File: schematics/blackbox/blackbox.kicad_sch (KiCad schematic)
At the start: 31 parts, among them J1 Micro_SD_Card, J104 SWD, J105 F_COMPUTER, J2 Micro_SD_Card, U101 MAX14787E, U102 STM32F405RGT6, Y101 26M

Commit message: Add power LED and test points
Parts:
- added D101: RED, Strix:LED_0402, symbol Strix:LED
- added R101: 50, Strix:R_0402, symbol Strix:R
- added TP101, TP102, TP103, TP104, TP105, TP106, TP107, TP108, TP109, TP110, TP111, TP112, TP113, TP114, TP115: TestPoint, Strix:TestPoint, symbol Strix:TestPoint
- renumbered C105 to C102, C107 to C103, C112 to C104, C102 to C105, C108 to C107, C109 to C108, C110 to C109, C111 to C110, C103 to C111, C104 to C112, D104 to D102, D105 to D103, D106 to D104, D107 to D105, D108 to D106, D109 to D107, J1 to J101, J2 to J102, J104 to J103, J105 to J104, R101 to R103, U102 to U101, U101 to U102
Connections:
- net 3v3: now also R101.2, TP109.1
- net GND: now also D101.1, TP112.1, TP113.1, TP114.1, TP115.1
- net SD1_~{CS}: now also TP101.1
- net SD2_~{CS}: now also TP102.1
- net SPI2_MISO: now also TP110.1
- net SPI2_MOSI: now also TP107.1
- net SPI2_SCLK: now also TP104.1
- net SPI3_MISO: now also TP111.1
- net SPI3_MOSI: now also TP108.1
- net SPI3_SCLK: now also TP105.1
- net USART3_RX: now also TP103.1
- net USART3_TX: now also TP106.1
- new net: D101.2, R101.1
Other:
- note added: "Power LED"
- note added: "Test Points"

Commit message: Final changes for manufacture (and silkscreen meme)
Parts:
- C101: Farnell 2496814 -> 1759436
- C104: Farnell 2426952 -> 2211173
- C111, C112: Farnell (none) -> 2494183
- J101, J102: Farnell (none) -> 1344008
- J103: Farnell (none) -> 2856426
- R101: Farnell (none) -> 3544456
- R102: Farnell (none) -> 2447095
- R103: Farnell (none) -> 2447103
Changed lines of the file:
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@@
       (effects (font (size 1.27 1.27)) hide)
     )
-    (property "Farnell" "2496814" (id 4) (at 76.2 66.04 0)
+    (property "Farnell" "1759436" (id 4) (at 76.2 66.04 0)
       (effects (font (size 1.27 1.27)) hide)
     )
@@
       (effects (font (size 1.27 1.27)) hide)
     )
-    (property "Farnell" "2426952" (id 4) (at 119.38 72.39 0)
+    (property "Farnell" "2211173" (id 4) (at 119.38 72.39 0)
       (effects (font (size 1.27 1.27)) hide)
     )
@@
     )
     (property "Datasheet" "~" (id 3) (at 146.05 179.07 0)
+      (effects (font (size 1.27 1.27)) hide)
+    )
+    (property "Farnell" "~" (id 4) (at 146.05 179.07 0)
       (effects (font (size 1.27 1.27)) hide)
     )
@@
       (effects (font (size 1.27 1.27)) hide)
     )
+    (property "Farnell" "~" (id 4) (at 153.67 179.07 0)
+      (effects (font (size 1.27 1.27)) hide)
+    )
     (pin "1")
   )
@@
       (effects (font (size 1.27 1.27)) hide)
     )
+    (property "Farnell" "~" (id 4) (at 161.29 179.07 0)
+      (effects (font (size 1.27 1.27)) hide)
+    )
     (pin "1")
   )
@@
     )
     (property "Datasheet" "~" (id 3) (at 168.91 179.07 0)
+      (effects (font (size 1.27 1.27)) hide)
+    )
+    (property "Farnell" "~" (id 4) (at 168.91 179.07 0)
       (effects (font (size 1.27 1.27)) hide)
     )
@@
       (effects (font (size 1.27 1.27)) hide)
     )
+    (property "Farnell" "2447103" (id 4) (at 53.34 177.8 0)
+      (effects (font (size 1.27 1.27)) hide)
+    )
     (pin "1")
     (pin "2")
@@
       (effects (font (size 1.27 1.27)) hide)
     )
+    (property "Farnell" "~" (id 4) (at 153.67 35.56 0)
+      (effects (font (size 1.27 1.27)) hide)
+    )
     (pin "1")
   )
@@
     )
     (property "Datasheet" "~" (id 3) (at 153.67 50.8 0)
+      (effects (font (size 1.27 1.27)) hide)
+    )
+    (property "Farnell" "~" (id 4) (at 153.67 45.72 0)
       (effects (font (size 1.27 1.27)) hide)
     )
@@
       (effects (font (size 1.27 1.27)) hide)
     )
+    (property "Farnell" "3544456" (id 4) (at 59.69 68.58 0)
+      (effects (font (size 1.27 1.27)) hide)
+    )
     (pin "1")
     (pin "2")
@@
     )
     (property "Datasheet" "~" (id 3) (at 153.67 48.26 0)
+      (effects (font (size 1.27 1.27)) hide)
+    )
+    (property "Farnell" "~" (id 4) (at 153.67 43.18 0)
       (effects (font (size 1.27 1.27)) hide)
     )
@@
     )
     (property "Datasheet" "http://katalog.we-online.de/em/datasheet/693072010801.pdf" (id 3) (at 224.79 123.19 0)
+      (effects (font (size 1.27 1.27)) hide)
+    )
+    (property "Farnell" "1344008" (id 4) (at 224.79 123.19 0)
       (effects (font (size 1.27 1.27)) hide)
     )
@@
       (effects (font (size 1.27 1.27)) hide)
     )
+    (property "Farnell" "2494183" (id 4) (at 81.28 113.03 0)
+      (effects (font (size 1.27 1.27)) hide)
+    )
     (pin "1")
     (pin "2")
@@
       (effects (font (size 1.27 1.27)) hide)
     )
+    (property "Farnell" "2447095" (id 4) (at 88.9 110.49 0)
+      (effects (font (size 1.27 1.27)) hide)
+    )
     (pin "1")
     (pin "2")
@@
       (effects (font (size 1.27 1.27)) hide)
     )
+    (property "Farnell" "~" (id 4) (at 92.71 40.64 0)
+      (effects (font (size 1.27 1.27)) hide)
+    )
     (pin "1")
   )
@@
       (effects (font (size 1.27 1.27)) hide)
     )
+    (property "Farnell" "~" (id 4) (at 153.67 40.64 0)
+      (effects (font (size 1.27 1.27)) hide)
+    )
     (pin "1")
   )
@@
     )
     (property "Datasheet" "~" (id 3) (at 92.71 50.8 0)
+      (effects (font (size 1.27 1.27)) hide)
+    )
+    (property "Farnell" "~" (id 4) (at 92.71 45.72 0)
       (effects (font (size 1.27 1.27)) hide)
     )
@@
       (effects (font (size 1.27 1.27)) hide)
     )
+    (property "Farnell" "~" (id 4) (at 123.19 45.72 0)
+      (effects (font (size 1.27 1.27)) hide)
+    )
     (pin "1")
   )
@@
     )
     (property "Datasheet" "~" (id 3) (at 92.71 43.18 0)
+      (effects (font (size 1.27 1.27)) hide)
+    )
+    (property "Farnell" "~" (id 4) (at 92.71 38.1 0)
       (effects (font (size 1.27 1.27)) hide)
     )
@@
     )
     (property "Datasheet" "http://katalog.we-online.de/em/datasheet/693072010801.pdf" (id 3) (at 224.79 83.82 0)
+      (effects (font (size 1.27 1.27)) hide)
+    )
+    (property "Farnell" "1344008" (id 4) (at 224.79 83.82 0)
       (effects (font (size 1.27 1.27)) hide)
     )
@@
       (effects (font (size 1.27 1.27)) hide)
     )
+    (property "Farnell" "~" (id 4) (at 123.19 40.64 0)
+      (effects (font (size 1.27 1.27)) hide)
+    )
     (pin "1")
   )
@@
       (effects (font (size 1.27 1.27)) hide)
     )
+    (property "Farnell" "~" (id 4) (at 123.19 35.56 0)
+      (effects (font (size 1.27 1.27)) hide)
+    )
     (pin "1")
   )
@@
     )
     (property "Datasheet" "~" (id 3) (at 123.19 43.18 0)
+      (effects (font (size 1.27 1.27)) hide)
+    )
+    (property "Farnell" "~" (id 4) (at 123.19 38.1 0)
       (effects (font (size 1.27 1.27)) hide)
     )
@@
       (effects (font (size 1.27 1.27)) hide)
     )
+    (property "Farnell" "2494183" (id 4) (at 81.28 102.87 0)
+      (effects (font (size 1.27 1.27)) hide)
+    )
     (pin "1")
     (pin "2")
@@
     )
     (property "Datasheet" "~" (id 3) (at 92.71 40.64 0)
+      (effects (font (size 1.27 1.27)) hide)
+    )
+    (property "Farnell" "~" (id 4) (at 92.71 35.56 0)
       (effects (font (size 1.27 1.27)) hide)
     )
@@
       (effects (font (size 1.27 1.27)) hide)
     )
+    (property "Farnell" "~" (id 4) (at 153.67 38.1 0)
+      (effects (font (size 1.27 1.27)) hide)
+    )
     (pin "1")
   )
@@
     )
     (property "Datasheet" "~" (id 3) (at 123.19 48.26 0)
+      (effects (font (size 1.27 1.27)) hide)
+    )
+    (property "Farnell" "~" (id 4) (at 123.19 43.18 0)
       (effects (font (size 1.27 1.27)) hide)
     )
@@
     )
     (property "Datasheet" "~" (id 3) (at 102.87 177.8 0)
+      (effects (font (size 1.27 1.27)) hide)
+    )
+    (property "Farnell" "~" (id 4) (at 102.87 177.8 0)
       (effects (font (size 1.27 1.27)) hide)
     )
@@
     )
     (property "Datasheet" "~" (id 3) (at 78.74 142.24 0)
+      (effects (font (size 1.27 1.27)) hide)
+    )
+    (property "Farnell" "2856426" (id 4) (at 78.74 142.24 0)
       (effects (font (size 1.27 1.27)) hide)
     )
@@
       (effects (font (size 1.27 1.27)) hide)
     )
+    (property "Farnell" "~" (id 4) (at 92.71 43.18 0)
+      (effects (font (size 1.27 1.27)) hide)
+    )

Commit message: Fix library references
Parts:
- J101, J102: footprint Connector_Card:microSD_HC_Wuerth_693072010801 -> Strix:microSD_HC_Wuerth_693072010801; symbol Connector:Micro_SD_Card -> Strix:Micro_SD_Card
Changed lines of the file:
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@@
     (pin "1")
   )
-  (symbol (lib_id "Connector:Micro_SD_Card") (at 224.79 123.19 0) (unit 1)
+  (symbol (lib_id "Strix:Micro_SD_Card") (at 224.79 123.19 0) (unit 1)
     (in_bom yes) (on_board yes) (fields_autoplaced)
     (property "Reference" "J102" (id 0) (at 225.425 104.14 0))
     (property "Value" "Micro_SD_Card" (id 1) (at 225.425 106.68 0))
-    (property "Footprint" "Connector_Card:microSD_HC_Wuerth_693072010801" (id 2) (at 254 115.57 0)
+    (property "Footprint" "Strix:microSD_HC_Wuerth_693072010801" (id 2) (at 254 115.57 0)
       (effects (font (size 1.27 1.27)) hide)
     )
@@
     (pin "1")
   )
-  (symbol (lib_id "Connector:Micro_SD_Card") (at 224.79 83.82 0) (unit 1)
+  (symbol (lib_id "Strix:Micro_SD_Card") (at 224.79 83.82 0) (unit 1)
     (in_bom yes) (on_board yes) (fields_autoplaced)
     (property "Reference" "J101" (id 0) (at 225.425 64.77 0))
     (property "Value" "Micro_SD_Card" (id 1) (at 225.425 67.31 0))
-    (property "Footprint" "Connector_Card:microSD_HC_Wuerth_693072010801" (id 2) (at 254 76.2 0)
+    (property "Footprint" "Strix:microSD_HC_Wuerth_693072010801" (id 2) (at 254 76.2 0)
       (effects (font (size 1.27 1.27)) hide)
     )
@@
     )
     (path "/b9cca626-7245-4480-a9b4-98fe421cf0c1"
-      (reference "J101") (unit 1) (value "Micro_SD_Card") (footprint "Connector_Card:microSD_HC_Wuerth_693072010801")
+      (reference "J101") (unit 1) (value "Micro_SD_Card") (footprint "Strix:microSD_HC_Wuerth_693072010801")
     )
     (path "/44234758-a0aa-4225-a0d7-15a67df397a1"
-      (reference "J102") (unit 1) (value "Micro_SD_Card") (footprint "Connector_Card:microSD_HC_Wuerth_693072010801")
+      (reference "J102") (unit 1) (value "Micro_SD_Card") (footprint "Strix:microSD_HC_Wuerth_693072010801")
     )
     (path "/e584c80e-3de9-4f7a-9e9d-844bd2086241"

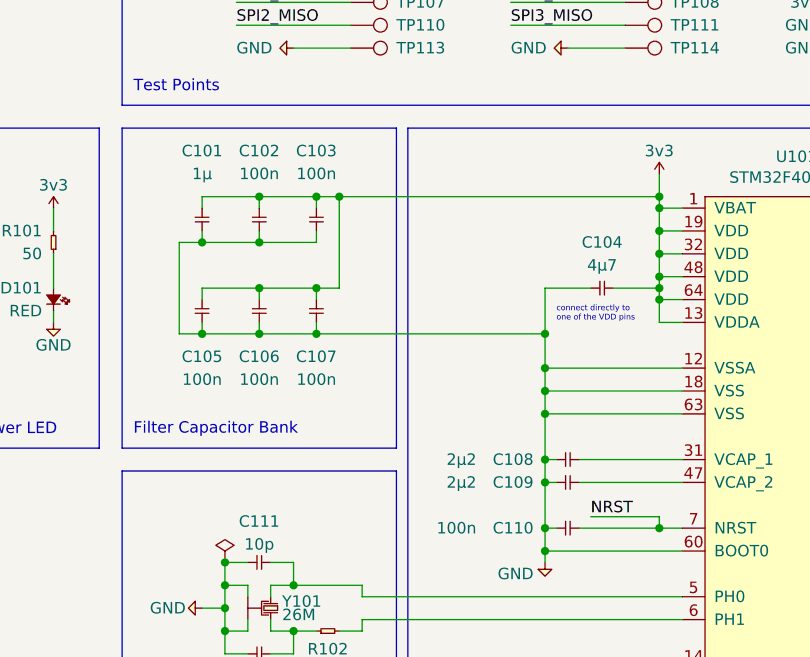
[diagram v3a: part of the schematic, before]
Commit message: Update passive order codes to 0402
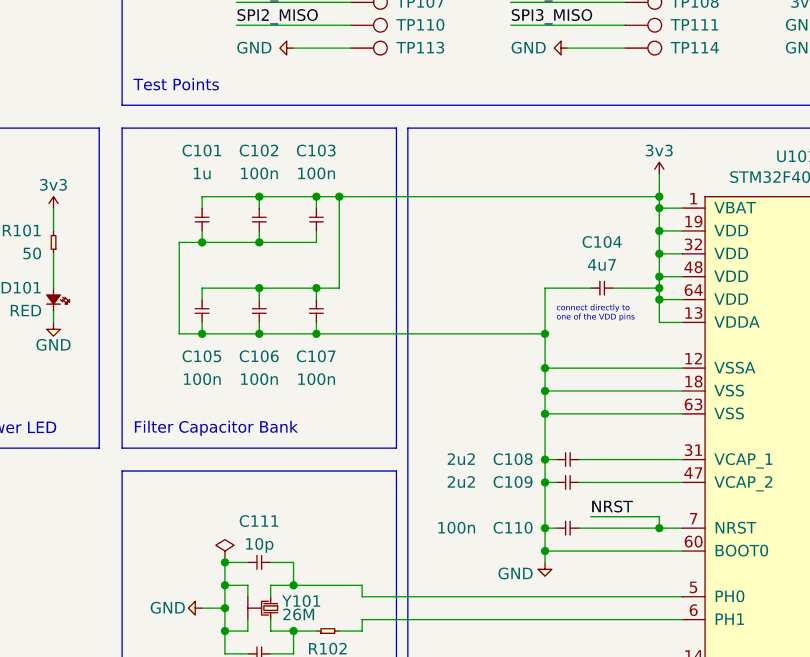
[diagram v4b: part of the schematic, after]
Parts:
- C101: value 1µ -> 1u; Farnell 1759436 -> 2218855
- C104: value 4µ7 -> 4u7; Farnell 2211173 -> 2346876
- C108, C109: value 2µ2 -> 2u2
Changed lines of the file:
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@@
       (effects (font (size 1.27 1.27)) (justify right))
     )
-    (property "Value" "2µ2" (id 1) (at 106.68 91.44 0)
+    (property "Value" "2u2" (id 1) (at 106.68 91.44 0)
       (effects (font (size 1.27 1.27)) (justify right))
     )
@@
       (effects (font (size 1.27 1.27)) (justify right))
     )
-    (property "Value" "2µ2" (id 1) (at 106.68 93.98 0)
+    (property "Value" "2u2" (id 1) (at 106.68 93.98 0)
       (effects (font (size 1.27 1.27)) (justify right))
     )
@@
     (in_bom yes) (on_board yes)
     (property "Reference" "C101" (id 0) (at 76.2 57.15 90))
-    (property "Value" "1µ" (id 1) (at 76.2 59.69 90))
+    (property "Value" "1u" (id 1) (at 76.2 59.69 90))
     (property "Footprint" "Strix:C_0402" (id 2) (at 76.2 66.04 0)
       (effects (font (size 1.27 1.27)) hide)
@@
       (effects (font (size 1.27 1.27)) hide)
     )
-    (property "Farnell" "1759436" (id 4) (at 76.2 66.04 0)
+    (property "Farnell" "2218855" (id 4) (at 76.2 66.04 0)
       (effects (font (size 1.27 1.27)) hide)
     )
@@
     (in_bom yes) (on_board yes)
     (property "Reference" "C104" (id 0) (at 120.65 67.31 0))
-    (property "Value" "4µ7" (id 1) (at 120.65 69.85 0))
+    (property "Value" "4u7" (id 1) (at 120.65 69.85 0))
     (property "Footprint" "Strix:C_0402" (id 2) (at 119.38 72.39 0)
       (effects (font (size 1.27 1.27)) hide)
@@
       (effects (font (size 1.27 1.27)) hide)
     )
-    (property "Farnell" "2211173" (id 4) (at 119.38 72.39 0)
+    (property "Farnell" "2346876" (id 4) (at 119.38 72.39 0)
       (effects (font (size 1.27 1.27)) hide)
     )
@@
     )
     (path "/00000000-0000-0000-0000-000060e7c4a9"
-      (reference "C101") (unit 1) (value "1µ") (footprint "Strix:C_0402")
+      (reference "C101") (unit 1) (value "1u") (footprint "Strix:C_0402")
     )
     (path "/00000000-0000-0000-0000-000060e7c4a2"
@@
     )
     (path "/00000000-0000-0000-0000-000060e7c4b0"
-      (reference "C104") (unit 1) (value "4µ7") (footprint "Strix:C_0402")
+      (reference "C104") (unit 1) (value "4u7") (footprint "Strix:C_0402")
     )
     (path "/00000000-0000-0000-0000-000060e7c494"
@@
     )
     (path "/00000000-0000-0000-0000-000060e7c46a"
-      (reference "C108") (unit 1) (value "2µ2") (footprint "Strix:C_0402")
+      (reference "C108") (unit 1) (value "2u2") (footprint "Strix:C_0402")
     )
     (path "/00000000-0000-0000-0000-000060e7c471"
-      (reference "C109") (unit 1) (value "2µ2") (footprint "Strix:C_0402")
+      (reference "C109") (unit 1) (value "2u2") (footprint "Strix:C_0402")
     )
     (path "/00000000-0000-0000-0000-0000613d0152"

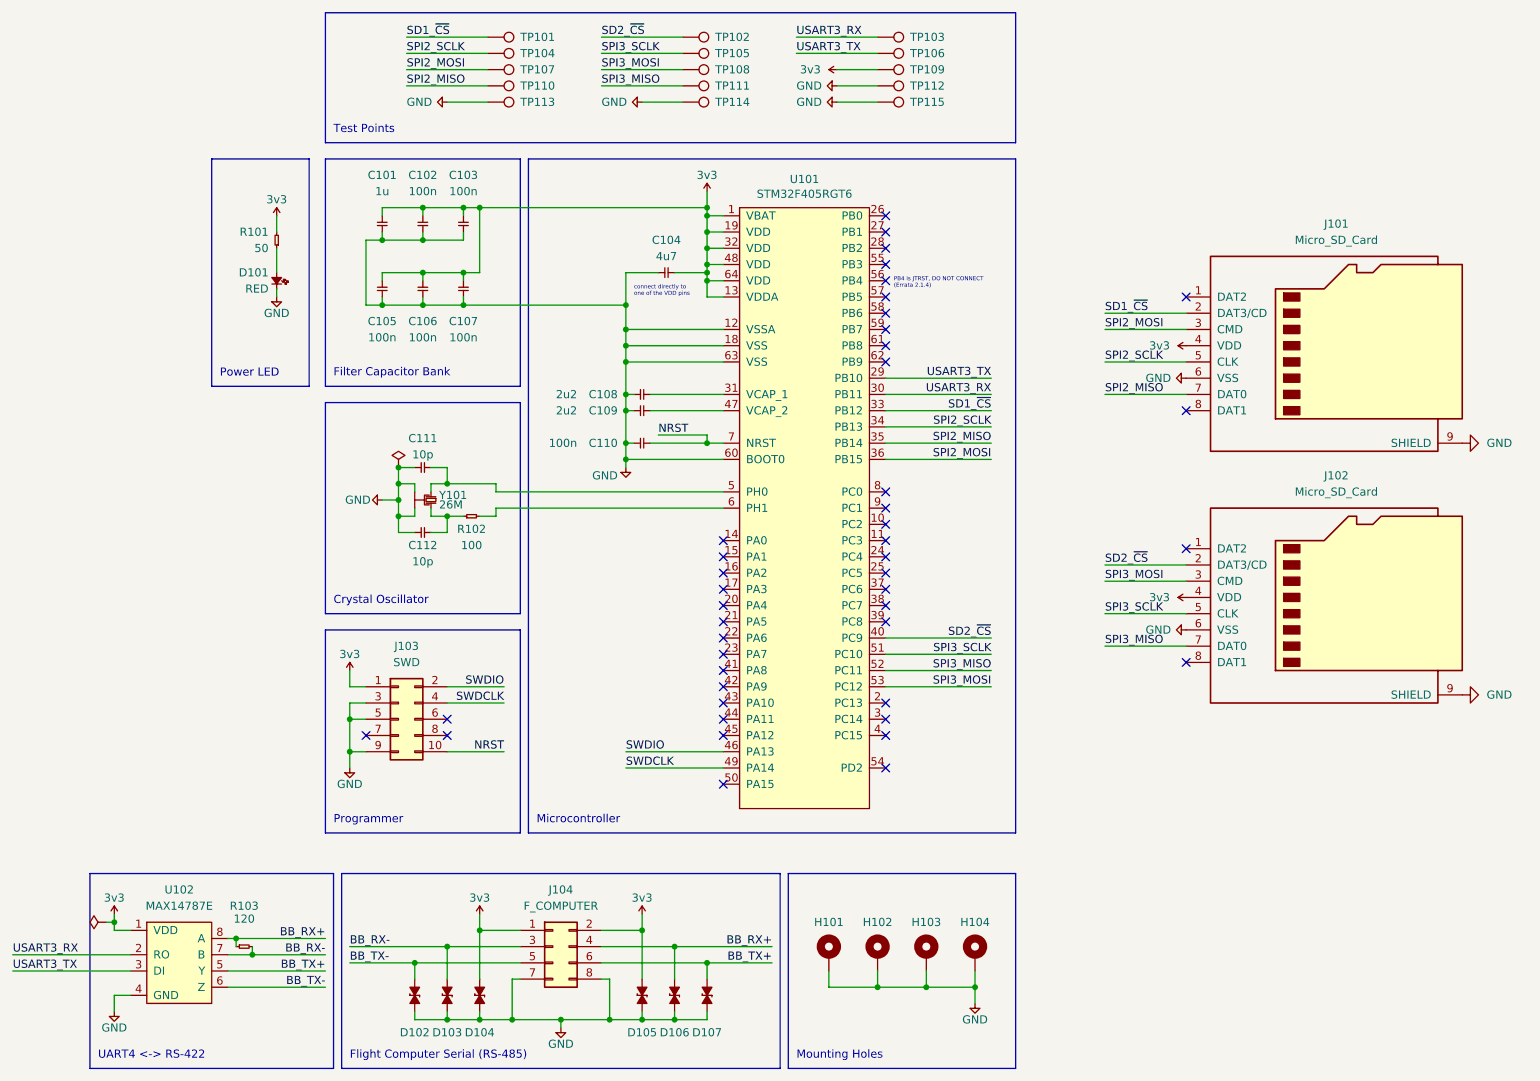
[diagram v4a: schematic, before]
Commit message: Minor changes to pass ERC
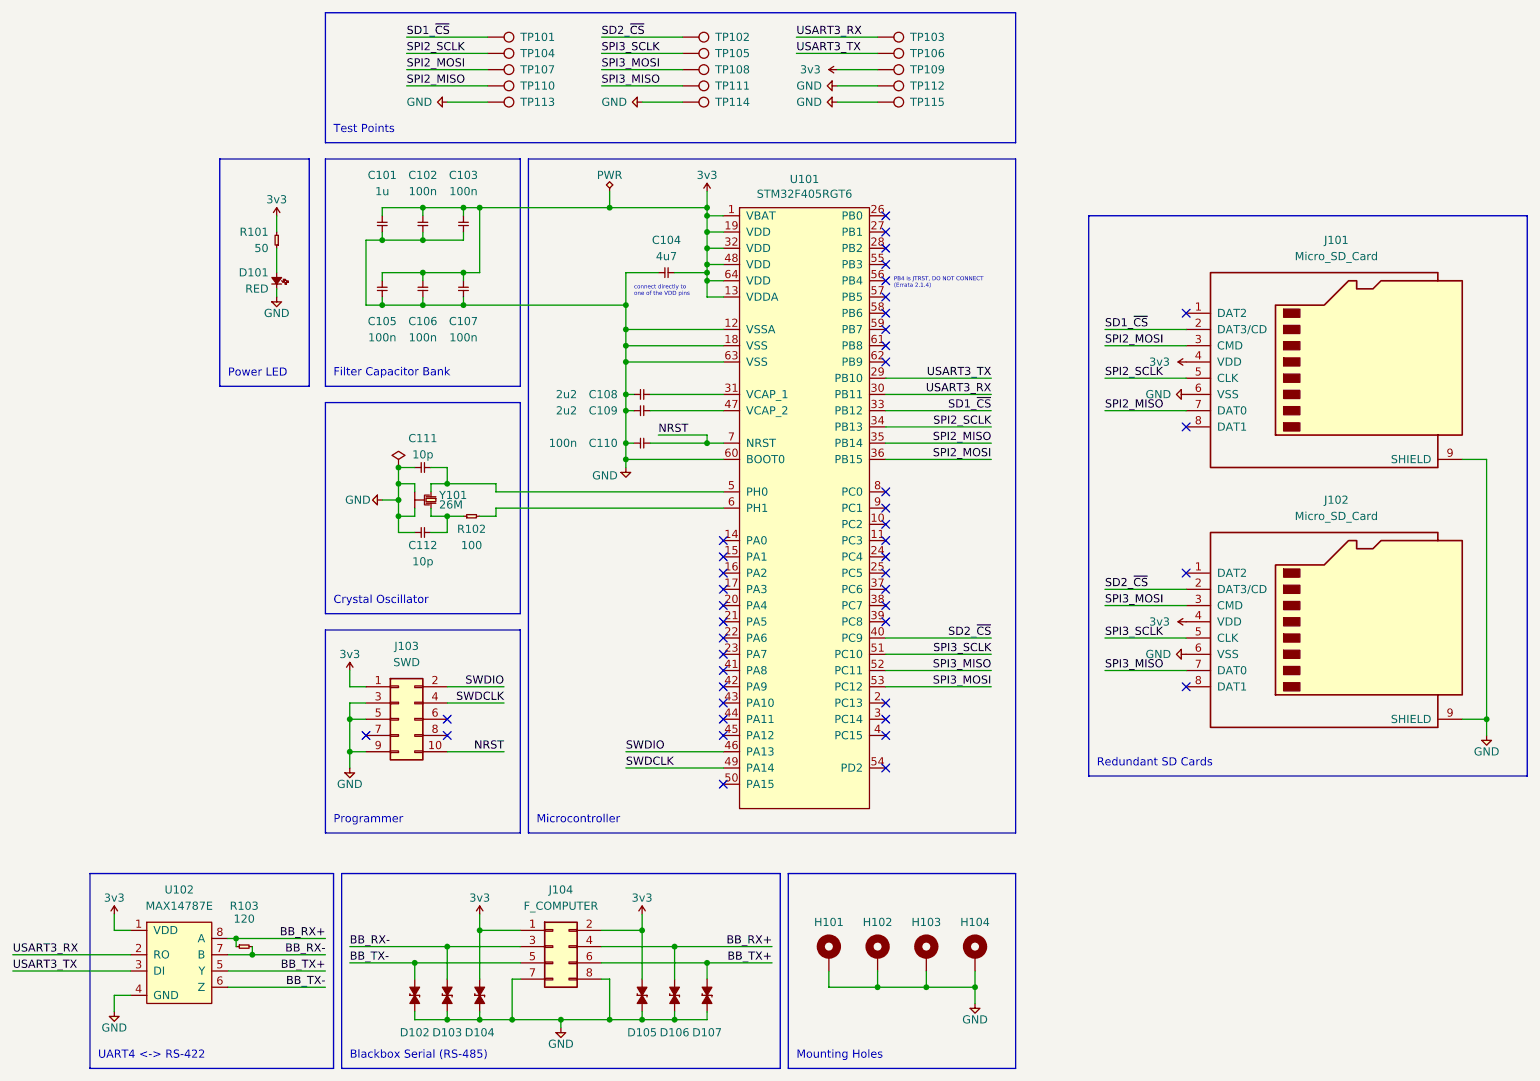
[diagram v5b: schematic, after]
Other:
- note added: "Blackbox Serial (RS-485)"
- note added: "Redundant SD Cards"
- note removed: "Flight Computer Serial (RS-485)"
- moved on the sheet: J101, J102
